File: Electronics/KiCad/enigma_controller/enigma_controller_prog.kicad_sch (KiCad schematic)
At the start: 13 parts, among them IC1 SN74LVC257ADR, IC10 MCP23017-E_SO, IC2 SN74LVC257ADR, IC3 SN74LVC257ADR, IC4 SN74LVC257ADR, IC5 SN74LVC257ADR, IC6 SN74LVC257ADR, IC7 SN74LVC257ADR, IC9 MCP23017-E_SO, J1 Conn_02x07_Odd_Even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

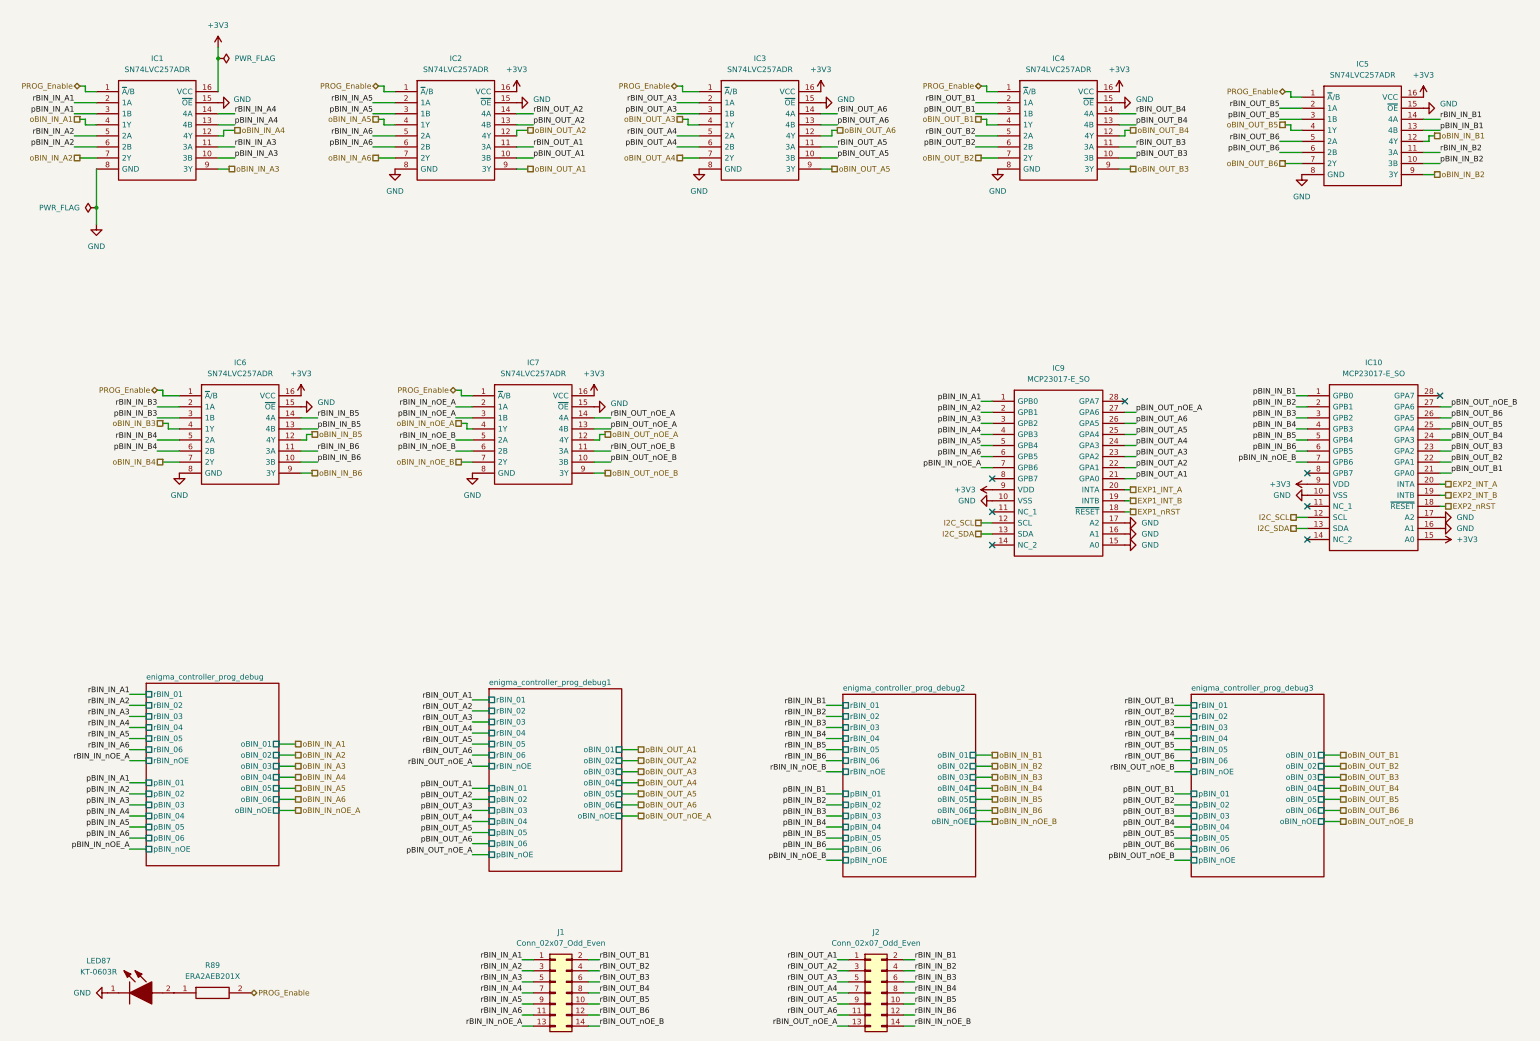
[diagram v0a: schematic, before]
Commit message: Refactored to remove debugger components.
Debug board is now a separate entity.
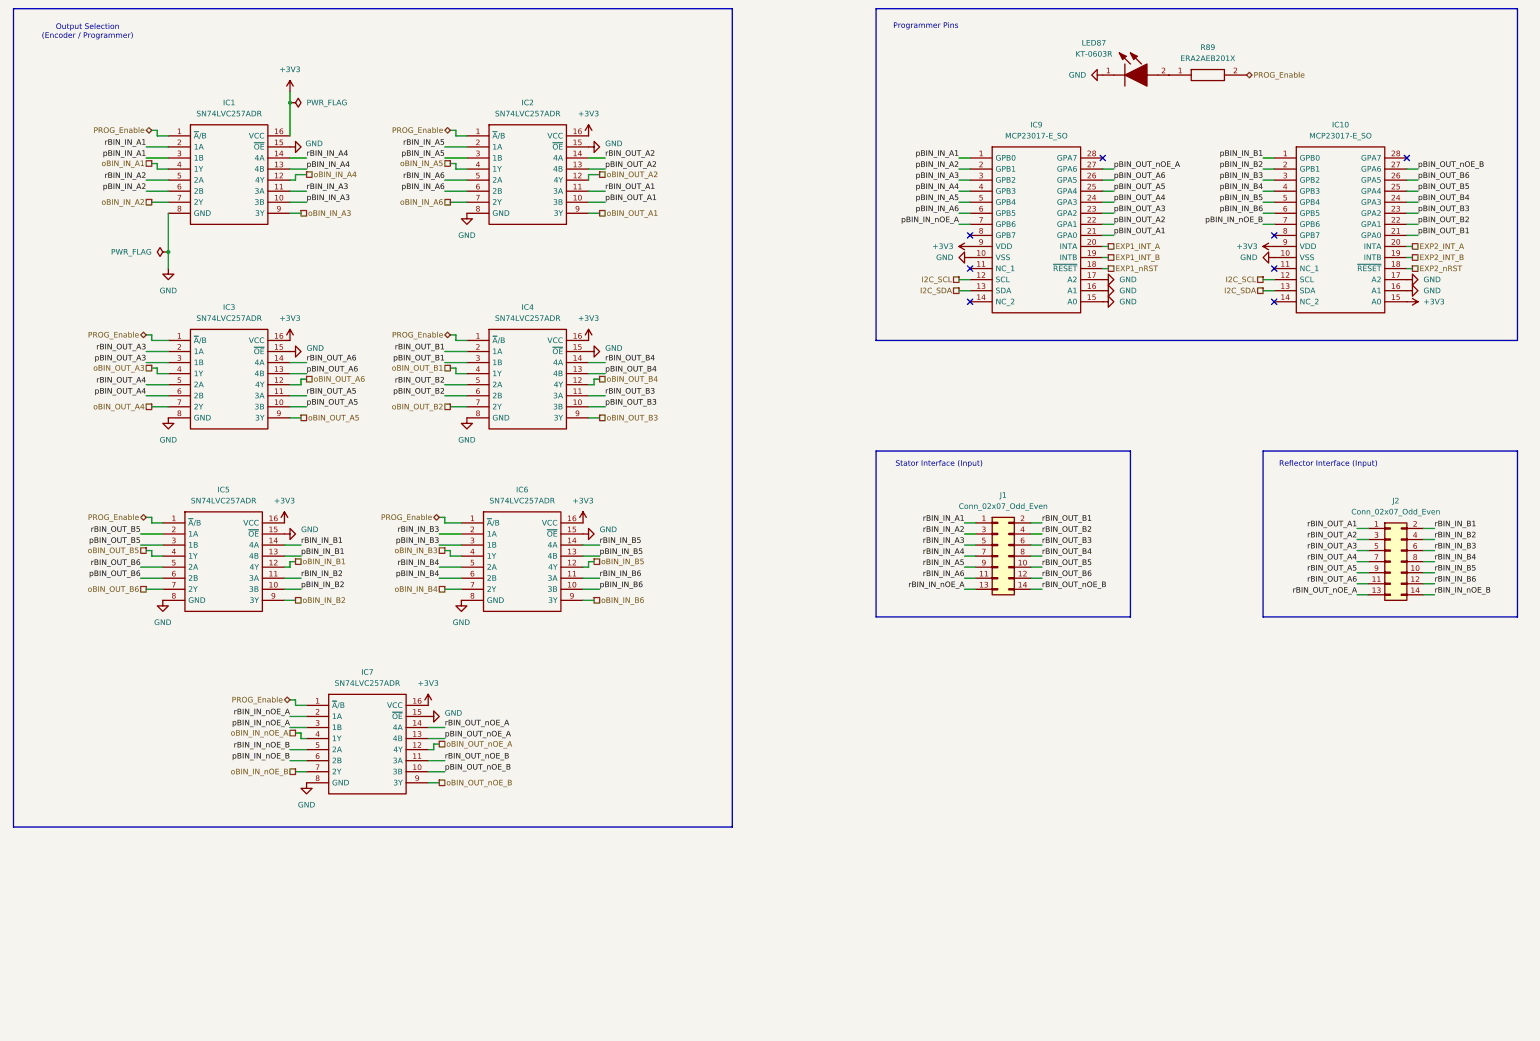
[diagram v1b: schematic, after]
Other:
- removed sheet enigma_controller_prog_debug
- removed sheet enigma_controller_prog_debug1
- removed sheet enigma_controller_prog_debug2
- removed sheet enigma_controller_prog_debug3
- note added: "Output Selection (Encoder / Programmer)"
- note added: "Programmer Pins"
- note added: "Reflector Interface (Input)"
- note added: "Stator Interface (Input)"
- company: (none) -> Enigmatic
- moved on the sheet: IC1, IC10, IC2, IC3, IC4, IC5, IC6, IC7, IC9, J1, J2, LED87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

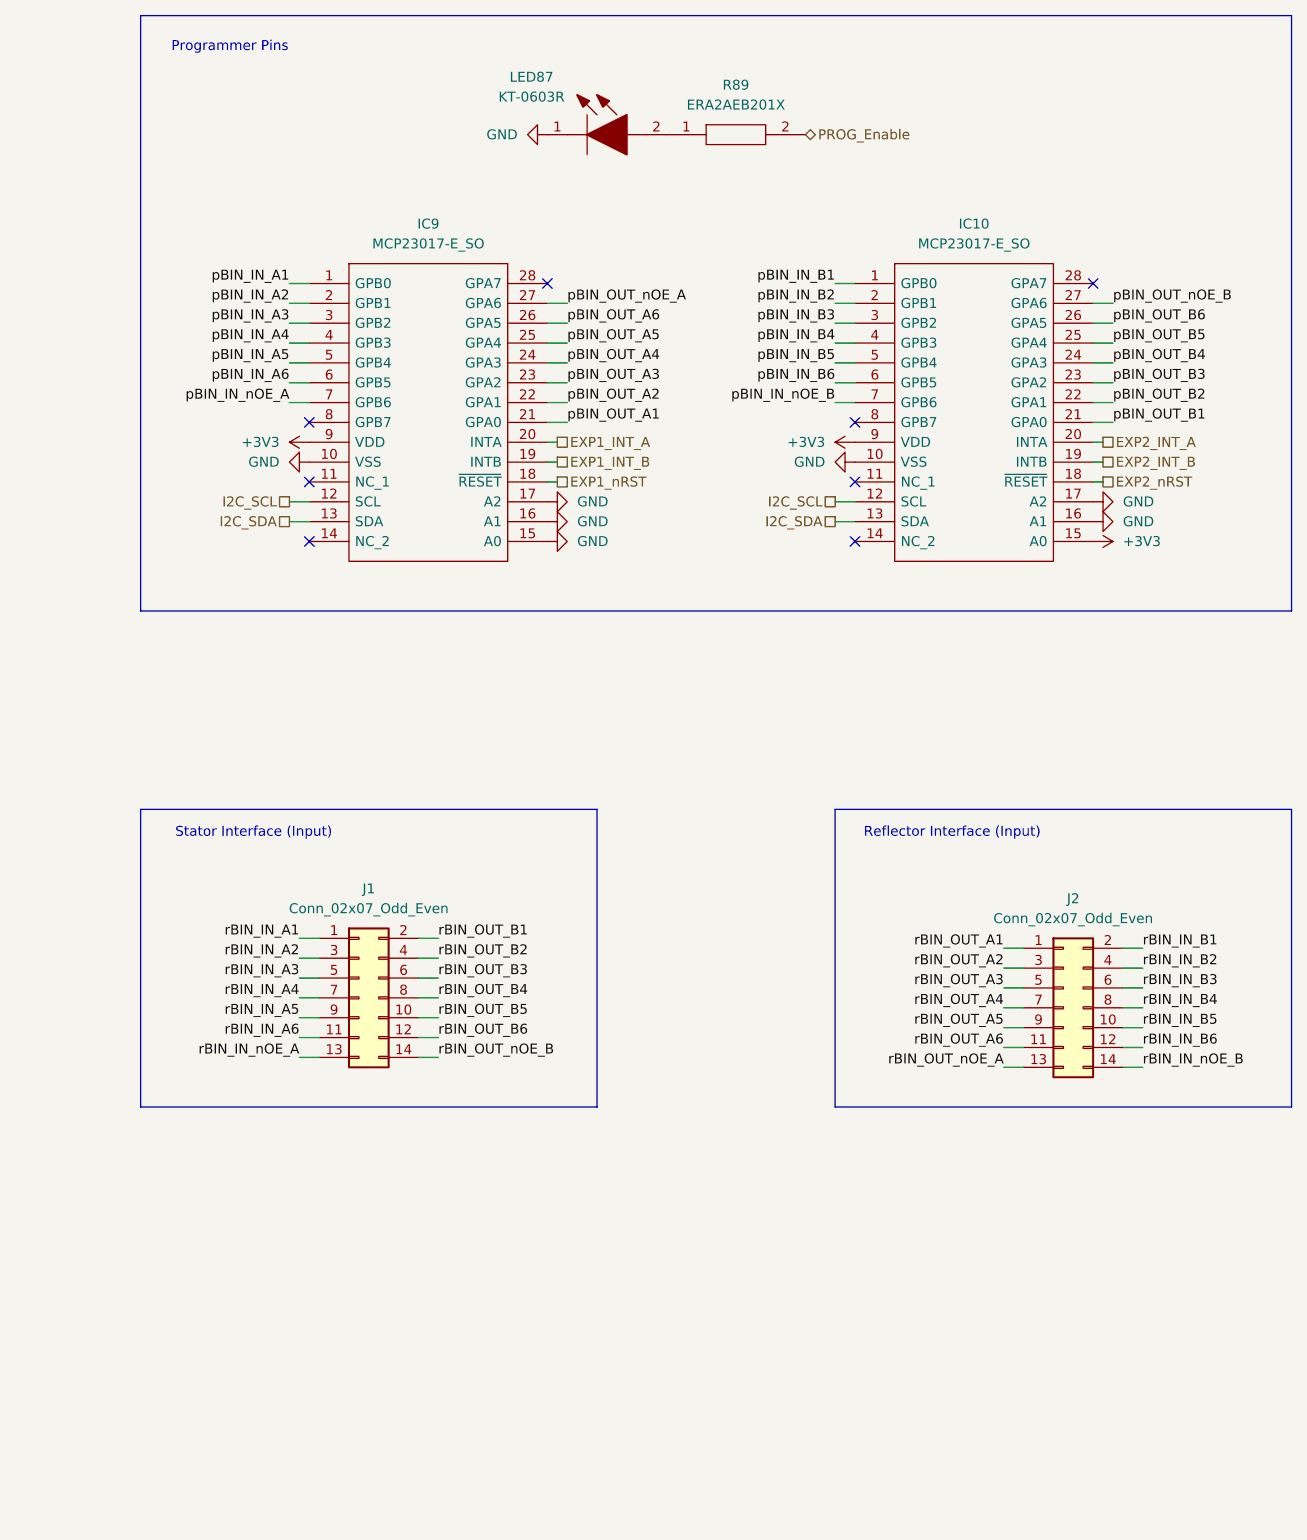
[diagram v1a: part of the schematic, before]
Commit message: Updates after TF review.
Added power regulators (CM5IO Schematic source).
Added decoupling caps.
Started replacing custom components with JLCPCB library variants.
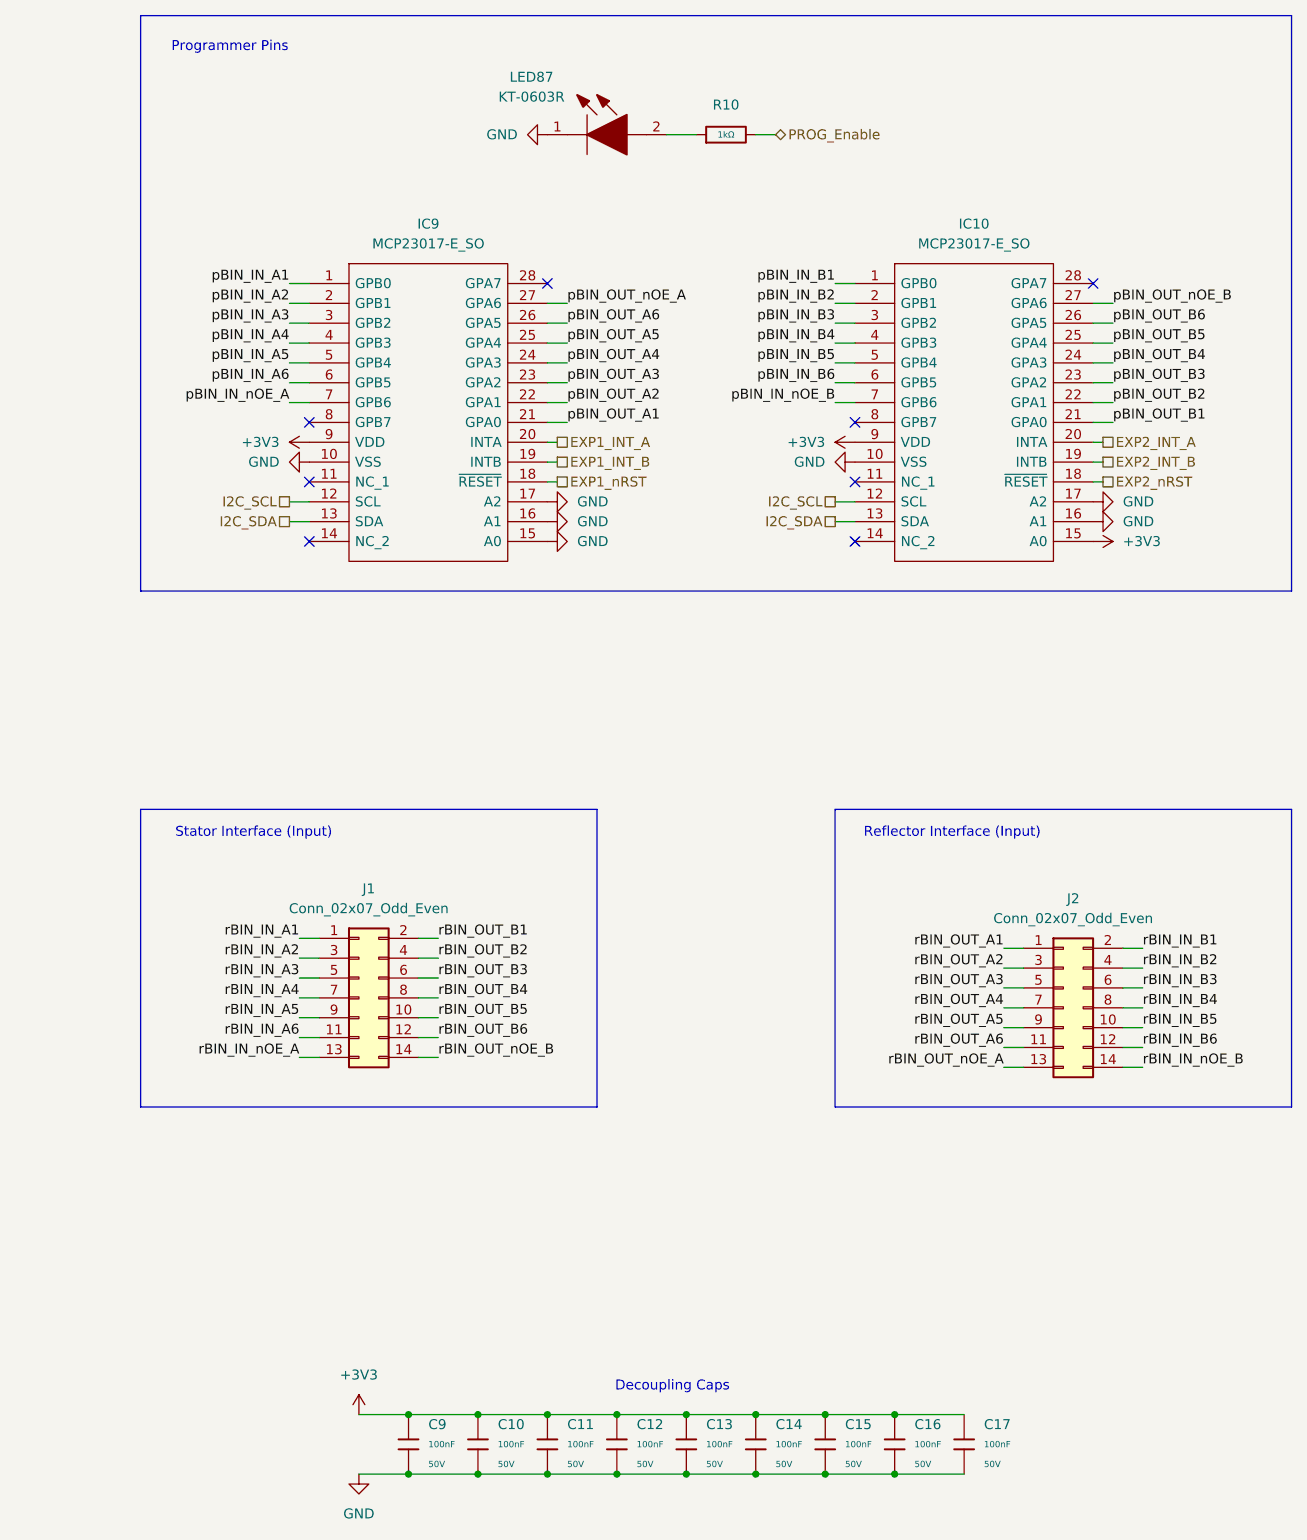
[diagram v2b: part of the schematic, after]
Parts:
- removed R89: ERA2AEB201X, Enigma_Components:ERA2AED122X, symbol Enigma_Components:ERA2AEB201X
- added C10, C11, C12, C13, C14, C15, C16, C17, C9: 100nF, PCM_JLCPCB:C_0402, symbol PCM_JLCPCB-Capacitors:0402,100nF,(2)
- added R10: 1kΩ, PCM_JLCPCB:R_0402, symbol PCM_JLCPCB-Resistors:0402,1kΩ
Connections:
- net +3V3: now also C10.1, C11.1, C12.1, C13.1, C14.1, C15.1, C16.1, C17.1, C9.1
- net GND: now also C10.2, C11.2, C12.2, C13.2, C14.2, C15.2, C16.2, C17.2, C9.2
- net PROG_Enable: now also R10.2
- net at LED87.2: now also R10.1
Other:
- note added: "Decoupling Caps"
